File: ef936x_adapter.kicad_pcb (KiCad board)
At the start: 2 copper layers, 25.4 x 55.9 mm, 5 parts, among them J1 Conn_01x20_Male, J2 Conn_01x20_Male, U1 EF9367, U2 74HC00, U3 74HC02

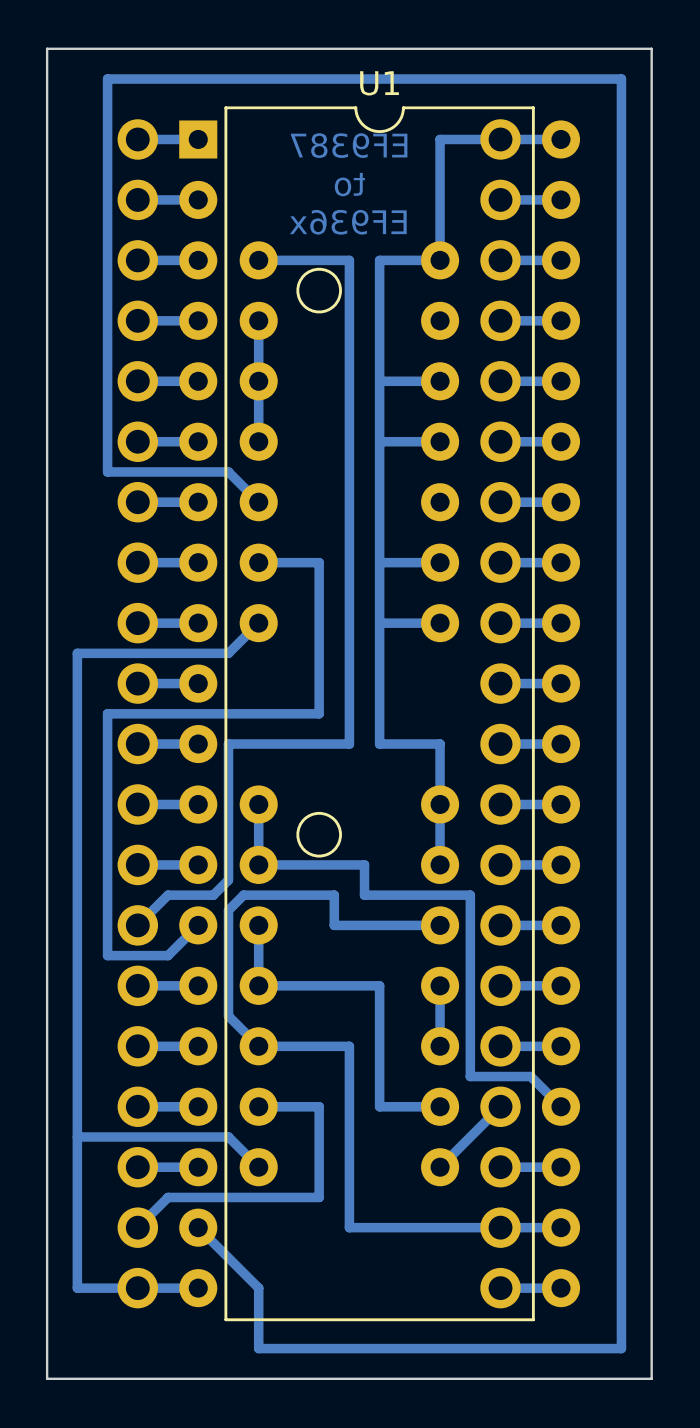
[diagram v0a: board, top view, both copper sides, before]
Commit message: Footprint fix
-footprint of EF9367 set to be a socket
-renamed schematic pdf file to be in line with other repos
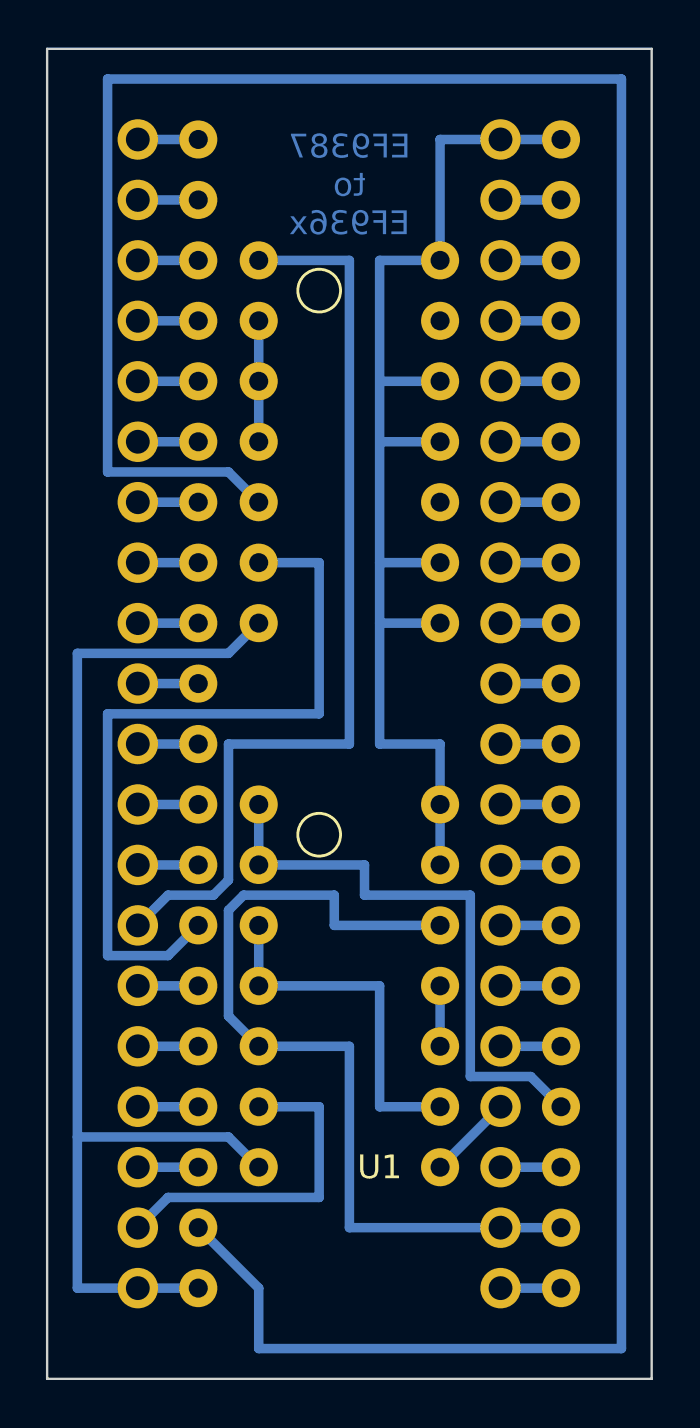
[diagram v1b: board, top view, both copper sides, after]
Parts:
- U1: footprint Package_DIP:DIP-40_W15.24mm -> ef936x_adapter_lib_fp:DIP-40_W15.24mm_Socket
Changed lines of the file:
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@@
     )
   )
-  (footprint "Package_DIP:DIP-40_W15.24mm" (layer "F.Cu")
+  (footprint "ef936x_adapter_lib_fp:DIP-40_W15.24mm_Socket" (layer "F.Cu")
     (at 114.3 50.8)
-    (descr "40-lead though-hole mounted DIP package, row spacing 15.24 mm (600 mils)")
-    (tags "THT DIP DIL PDIP 2.54mm 15.24mm 600mil")
+    (descr "40-lead though-hole mounted DIP package, row spacing 15.24 mm (600 mils), Socket")
+    (tags "THT DIP DIL PDIP 2.54mm 15.24mm 600mil Socket")
     (property "Sheetfile" "ef936x_adapter.kicad_sch")
     (property "Sheetname" "")
@@
     (property "ki_keywords" "Graphic Display Processor")
     (attr through_hole)
-    (fp_text reference "U1" (at 7.62 -2.33) (layer "F.SilkS")
+    (fp_text reference "U1" (at 7.62 43.18) (layer "F.SilkS")
         (effects (font (size 1 1) (thickness 0.15)))
     )
@@
         (effects (font (size 1 1) (thickness 0.15)))
     )
-    (fp_line (start 1.16 -1.33) (end 1.16 49.59)
-      (stroke (width 0.12) (type solid)) (layer "F.SilkS"))
-    (fp_line (start 1.16 49.59) (end 14.08 49.59)
-      (stroke (width 0.12) (type solid)) (layer "F.SilkS"))
-    (fp_line (start 6.62 -1.33) (end 1.16 -1.33)
-      (stroke (width 0.12) (type solid)) (layer "F.SilkS"))
-    (fp_line (start 14.08 -1.33) (end 8.62 -1.33)
-      (stroke (width 0.12) (type solid)) (layer "F.SilkS"))
-    (fp_line (start 14.08 49.59) (end 14.08 -1.33)
-      (stroke (width 0.12) (type solid)) (layer "F.SilkS"))
-    (fp_arc (start 8.62 -1.33) (mid 7.62 -0.33) (end 6.62 -1.33)
-      (stroke (width 0.12) (type solid)) (layer "F.SilkS"))
-    (fp_line (start -1.05 -1.55) (end -1.05 49.8)
+    (fp_line (start -1.55 -1.6) (end -1.55 49.85)
       (stroke (width 0.05) (type solid)) (layer "F.CrtYd"))
-    (fp_line (start -1.05 49.8) (end 16.3 49.8)
+    (fp_line (start -1.55 49.85) (end 16.8 49.85)
       (stroke (width 0.05) (type solid)) (layer "F.CrtYd"))
-    (fp_line (start 16.3 -1.55) (end -1.05 -1.55)
+    (fp_line (start 16.8 -1.6) (end -1.55 -1.6)
       (stroke (width 0.05) (type solid)) (layer "F.CrtYd"))
-    (fp_line (start 16.3 49.8) (end 16.3 -1.55)
+    (fp_line (start 16.8 49.85) (end 16.8 -1.6)
       (stroke (width 0.05) (type solid)) (layer "F.CrtYd"))
+    (fp_line (start -1.27 -1.33) (end -1.27 49.59)
+      (stroke (width 0.1) (type solid)) (layer "F.Fab"))
+    (fp_line (start -1.27 49.59) (end 16.51 49.59)
+      (stroke (width 0.1) (type solid)) (layer "F.Fab"))
     (fp_line (start 0.255 -0.27) (end 1.255 -1.27)
       (stroke (width 0.1) (type solid)) (layer "F.Fab"))
@@
     (fp_line (start 14.985 49.53) (end 0.255 49.53)
       (stroke (width 0.1) (type solid)) (layer "F.Fab"))
-    (pad "1" thru_hole rect (at 0 0) (size 1.6 1.6) (drill 0.8) (layers "*.Cu" "*.Mask")
+    (fp_line (start 16.51 -1.33) (end -1.27 -1.33)
+      (stroke (width 0.1) (type solid)) (layer "F.Fab"))
+    (fp_line (start 16.51 49.59) (end 16.51 -1.33)
+      (stroke (width 0.1) (type solid)) (layer "F.Fab"))
+    (pad "1" thru_hole circle (at 0 0) (size 1.6 1.6) (drill 0.8) (layers "*.Cu" "*.Mask")
       (net 1 "/CK") (pinfunction "CK") (pintype "input"))
     (pad "2" thru_hole oval (at 0 2.54) (size 1.6 1.6) (drill 0.8) (layers "*.Cu" "*.Mask")
@@
     (pad "40" thru_hole oval (at 15.24 0) (size 1.6 1.6) (drill 0.8) (layers "*.Cu" "*.Mask")
       (net 40 "+5V") (pinfunction "VCC") (pintype "power_in"))
-    (model "${KICAD6_3DMODEL_DIR}/Package_DIP.3dshapes/DIP-40_W15.24mm.wrl"
+    (model "${KIPRJMOD}/ef936x_adapter_lib_fp.3dshapes/40pin_socket.x3d"
       (offset (xyz 0 0 0))
       (scale (xyz 1 1 1))

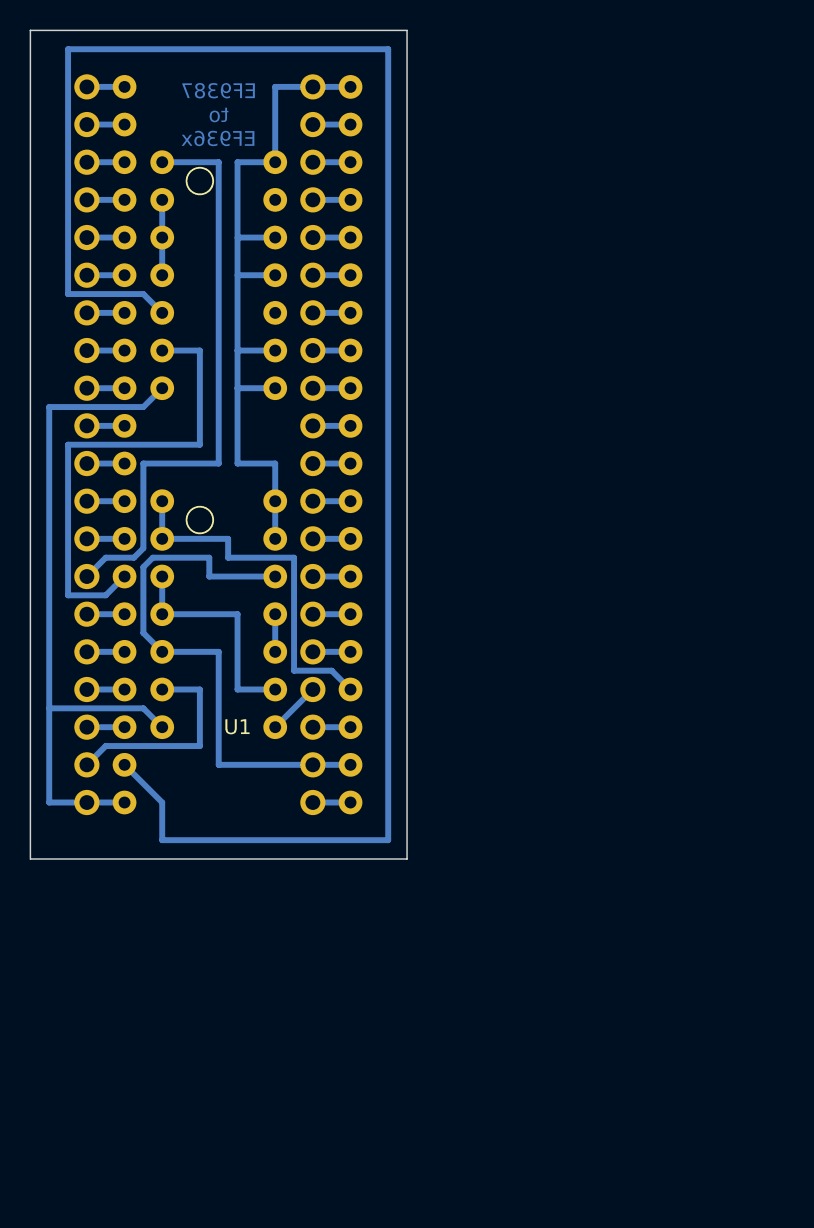
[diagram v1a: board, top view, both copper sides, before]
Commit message: no soldermask version
added a gerber containing masked out soldermaks for a vintage look
(works with pcb manufacturers that have no option to turn of soldermask)
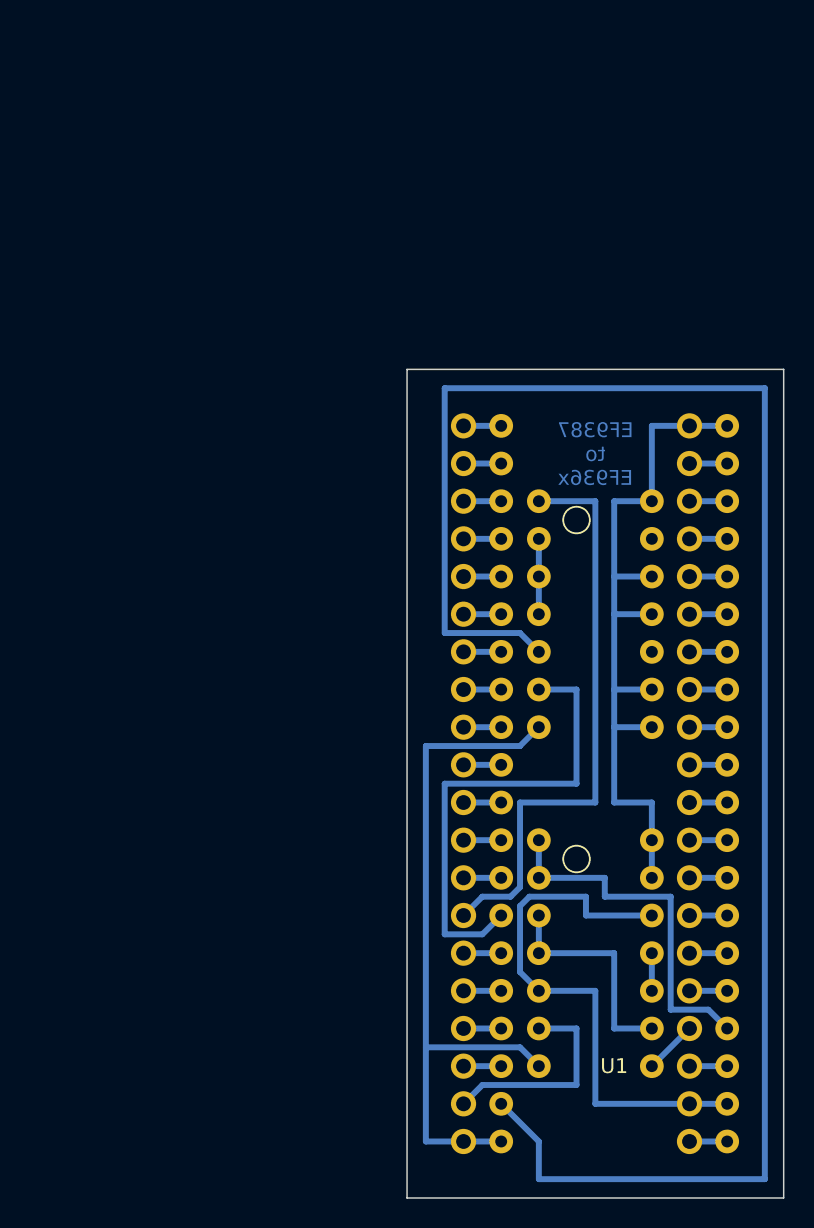
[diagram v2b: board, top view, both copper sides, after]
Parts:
- moved J2 34.2 mm to (152.4, 121.9)
- moved U2 34.2 mm to (142.2, 101.6)
- moved U3 34.2 mm to (142.2, 78.7)
- moved J1 34.2 mm to (137.2, 73.7)
- moved U1 34.2 mm to (139.7, 73.7)
